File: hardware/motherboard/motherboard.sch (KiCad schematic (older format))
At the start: 21 parts, among them J1 DB37_Female, J10 DB37_Female, J11 DB37_Female, J12 Barrel_Jack, J13 TSR 1-2433, J2 DB37_Female, J3 DB37_Female, J4 DB37_Female, J5 DB37_Female, J6 DB25_Female, J7 DB37_Female, J8 DB25_Female, J9 DB9_Female, SW1 SW_SPST

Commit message: All boards as fabbed at v1.0
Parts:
- added D1, D10, D11, D12, D13, D14, D15, D16, D17, D2, D3, D4, D5, D6, D7, D8, D9: LED, LED_SMD:LED_1206_3216Metric, symbol Device:LED
- added R10, R11, R12, R13, R14, R15, R16, R17, R18, R19, R3, R4, R5, R6, R7, R8, R9: 1K, Resistor_SMD:R_1206_3216Metric, symbol Device:R_US
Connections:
- net GND: now also R10.1, R11.1, R12.1, R13.1, R14.1, R15.1, R16.1, R17.1, R18.1, R19.1, R3.1, R4.1, R5.1, R6.1, R7.1, R8.1, R9.1
- net inst_0: now also D1.2 (A)
- net inst_1: now also D2.2 (A)
- net inst_10: now also D11.2 (A)
- net inst_11: now also D12.2 (A)
- net inst_12: now also D13.2 (A)
- net inst_13: now also D14.2 (A)
- net inst_14: now also D15.2 (A)
- net inst_15: now also D16.2 (A)
- net inst_2: now also D3.2 (A)
- net inst_3: now also D4.2 (A)
- net inst_4: now also D5.2 (A)
- net inst_5: now also D6.2 (A)
- net inst_6: now also D7.2 (A)
- net inst_7: now also D8.2 (A)
- net inst_8: now also D9.2 (A)
- net inst_9: now also D10.2 (A)
- new net: D1.1 (K), R3.2
- new net: D2.1 (K), R4.2
- new net: D3.1 (K), R5.2
- new net: D4.1 (K), R6.2
- new net: D5.1 (K), R7.2
- new net: D6.1 (K), R8.2
- new net: D7.1 (K), R9.2
- new net: D8.1 (K), R10.2
- new net: D9.1 (K), R11.2
- new net: D10.1 (K), R12.2
- new net: D11.1 (K), R13.2
- new net: D12.1 (K), R14.2
- new net: D13.1 (K), R15.2
- new net: D14.1 (K), R16.2
- new net: D15.1 (K), R17.2
- new net: D16.1 (K), R18.2
- new net: D17.1 (K), R19.2
- new net ~inst_15: D17.2 (A)
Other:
- note added: "Instruction LEDs"

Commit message: Motherboard: Added power switch, moved reset switch, modified silkscreens for readability, fixed A-register connector pinout, grounded NC input pins, changed paste layer clearance to -0.05mm
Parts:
- added SW2: SW_SPST, nandirl logo:SPST Toggle Switch, symbol Switch:SW_SPST
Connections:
- net Vin: now also SW2.2 (B); no longer C1.1, J12.1
- net areg_in0: now also J1.18; no longer J1.27
- net areg_in1: now also J1.36; no longer J1.8
- net areg_in10: now also J1.13; no longer J1.22
- net areg_in11: now also J1.31; no longer J1.3
- net areg_in12: now also J1.12; no longer J1.21
- net areg_in13: now also J1.30; no longer J1.2
- net areg_in14: now also J1.11; no longer J1.20
- net areg_in15: now also J1.29; no longer J1.1
- net areg_in2: now also J1.17; no longer J1.26
- net areg_in3: now also J1.35; no longer J1.7
- net areg_in4: now also J1.16; no longer J1.25
- net areg_in5: now also J1.34; no longer J1.6
- net areg_in6: now also J1.15; no longer J1.24
- net areg_in7: now also J1.33; no longer J1.5
- net areg_in8: now also J1.14; no longer J1.23
- net areg_in9: now also J1.32; no longer J1.4
- net areg_out0: now also J1.1; no longer J1.29
- net areg_out1: now also J1.20; no longer J1.11
- net areg_out10: now also J1.6; no longer J1.34
- net areg_out11: now also J1.25; no longer J1.16
- net areg_out12: now also J1.7; no longer J1.35
- net areg_out13: now also J1.26; no longer J1.17
- net areg_out14: now also J1.8; no longer J1.36
- net areg_out15: now also J1.27; no longer J1.18
- net areg_out2: now also J1.2; no longer J1.30
- net areg_out3: now also J1.21; no longer J1.12
- net areg_out4: now also J1.3; no longer J1.31
- net areg_out5: now also J1.22; no longer J1.13
- net areg_out6: now also J1.4; no longer J1.32
- net areg_out7: now also J1.23; no longer J1.14
- net areg_out8: now also J1.5; no longer J1.33
- net areg_out9: now also J1.24; no longer J1.15
- new net: C1.1, J12.1, SW2.1 (A)
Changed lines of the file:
@@
 	1    0    0    -1
 $EndComp
-Text GLabel 13650 3000 0    50   Output ~ 0
+Text GLabel 13650 1100 0    50   Output ~ 0
 areg_out0
-Text GLabel 13650 3100 0    50   Output ~ 0
+Text GLabel 13650 1200 0    50   Output ~ 0
 areg_out1
-Text GLabel 13650 3200 0    50   Output ~ 0
+Text GLabel 13650 1300 0    50   Output ~ 0
 areg_out2
-Text GLabel 13650 3300 0    50   Output ~ 0
+Text GLabel 13650 1400 0    50   Output ~ 0
 areg_out3
-Text GLabel 13650 3400 0    50   Output ~ 0
+Text GLabel 13650 1500 0    50   Output ~ 0
 areg_out4
-Text GLabel 13650 3500 0    50   Output ~ 0
+Text GLabel 13650 1600 0    50   Output ~ 0
 areg_out5
-Text GLabel 13650 3600 0    50   Output ~ 0
+Text GLabel 13650 1700 0    50   Output ~ 0
 areg_out6
-Text GLabel 13650 3700 0    50   Output ~ 0
+Text GLabel 13650 1800 0    50   Output ~ 0
 areg_out7
-Text GLabel 13650 3800 0    50   Output ~ 0
+Text GLabel 13650 1900 0    50   Output ~ 0
 areg_out8
-Text GLabel 13650 3900 0    50   Output ~ 0
+Text GLabel 13650 2000 0    50   Output ~ 0
 areg_out9
-Text GLabel 13650 4000 0    50   Output ~ 0
+Text GLabel 13650 2100 0    50   Output ~ 0
 areg_out10
-Text GLabel 13650 4100 0    50   Output ~ 0
+Text GLabel 13650 2200 0    50   Output ~ 0
 areg_out11
-Text GLabel 13650 4200 0    50   Output ~ 0
+Text GLabel 13650 2300 0    50   Output ~ 0
 areg_out12
-Text GLabel 13650 4300 0    50   Output ~ 0
+Text GLabel 13650 2400 0    50   Output ~ 0
 areg_out13
-Text GLabel 13650 4400 0    50   Output ~ 0
+Text GLabel 13650 2500 0    50   Output ~ 0
 areg_out14
-Text GLabel 13650 4500 0    50   Output ~ 0
+Text GLabel 13650 2600 0    50   Output ~ 0
 areg_out15
-Text GLabel 13650 4500 0    50   Output ~ 0
+Text GLabel 13650 2600 0    50   Output ~ 0
 areg_out15
 $Comp
@@
 	13650 2800 13650 2700
 Connection ~ 13650 2700
-Text GLabel 13650 2600 0    50   Input ~ 0
+Text GLabel 13650 4500 0    50   Input ~ 0
 areg_in0
-Text GLabel 13650 2500 0    50   Input ~ 0
+Text GLabel 13650 4400 0    50   Input ~ 0
 areg_in1
-Text GLabel 13650 2400 0    50   Input ~ 0
+Text GLabel 13650 4300 0    50   Input ~ 0
 areg_in2
-Text GLabel 13650 2300 0    50   Input ~ 0
+Text GLabel 13650 4200 0    50   Input ~ 0
 areg_in3
-Text GLabel 13650 2200 0    50   Input ~ 0
+Text GLabel 13650 4100 0    50   Input ~ 0
 areg_in4
-Text GLabel 13650 2100 0    50   Input ~ 0
+Text GLabel 13650 4000 0    50   Input ~ 0
 areg_in5
-Text GLabel 13650 2000 0    50   Input ~ 0
+Text GLabel 13650 3900 0    50   Input ~ 0
 areg_in6
-Text GLabel 13650 1900 0    50   Input ~ 0
+Text GLabel 13650 3800 0    50   Input ~ 0
 areg_in7
-Text GLabel 13650 1800 0    50   Input ~ 0
+Text GLabel 13650 3700 0    50   Input ~ 0
 areg_in8
-Text GLabel 13650 1700 0    50   Input ~ 0
+Text GLabel 13650 3600 0    50   Input ~ 0
 areg_in9
-Text GLabel 13650 1600 0    50   Input ~ 0
+Text GLabel 13650 3500 0    50   Input ~ 0
 areg_in10
-Text GLabel 13650 1500 0    50   Input ~ 0
+Text GLabel 13650 3400 0    50   Input ~ 0
 areg_in11
-Text GLabel 13650 1400 0    50   Input ~ 0
+Text GLabel 13650 3300 0    50   Input ~ 0
 areg_in12
-Text GLabel 13650 1300 0    50   Input ~ 0
+Text GLabel 13650 3200 0    50   Input ~ 0
 areg_in13
-Text GLabel 13650 1200 0    50   Input ~ 0
+Text GLabel 13650 3100 0    50   Input ~ 0
 areg_in14
-Text GLabel 13650 1100 0    50   Input ~ 0
+Text GLabel 13650 3000 0    50   Input ~ 0
 areg_in15
 Text GLabel 13650 4600 0    50   Input ~ 0
@@
 	1    0    0    -1
 $EndComp
-Text GLabel 9350 9550 2    50   Output ~ 0
+Text GLabel 9900 9550 2    50   Output ~ 0
 Vin
 Wire Wire Line
@@
 Text Notes 9650 5650 2    50   ~ 0
 Instruction LEDs
+$Comp
+L Switch:SW_SPST SW2
+U 1 1 5EDCC3F6
+P 9550 9550
+F 0 "SW2" H 9550 9785 50  0000 C CNN
+F 1 "SW_SPST" H 9550 9694 50  0000 C CNN
+F 2 "nandirl logo:SPST Toggle Switch" H 9550 9550 50  0001 C CNN
+F 3 "~" H 9550 9550 50  0001 C CNN
+F 4 "EG4914-ND" H 9550 9550 50  0001 C CNN "Digikey PN"
+	1    9550 9550
+	1    0    0    -1
+$EndComp
+Wire Wire Line
+	9750 9550 9900 9550
 $EndSCHEMATC

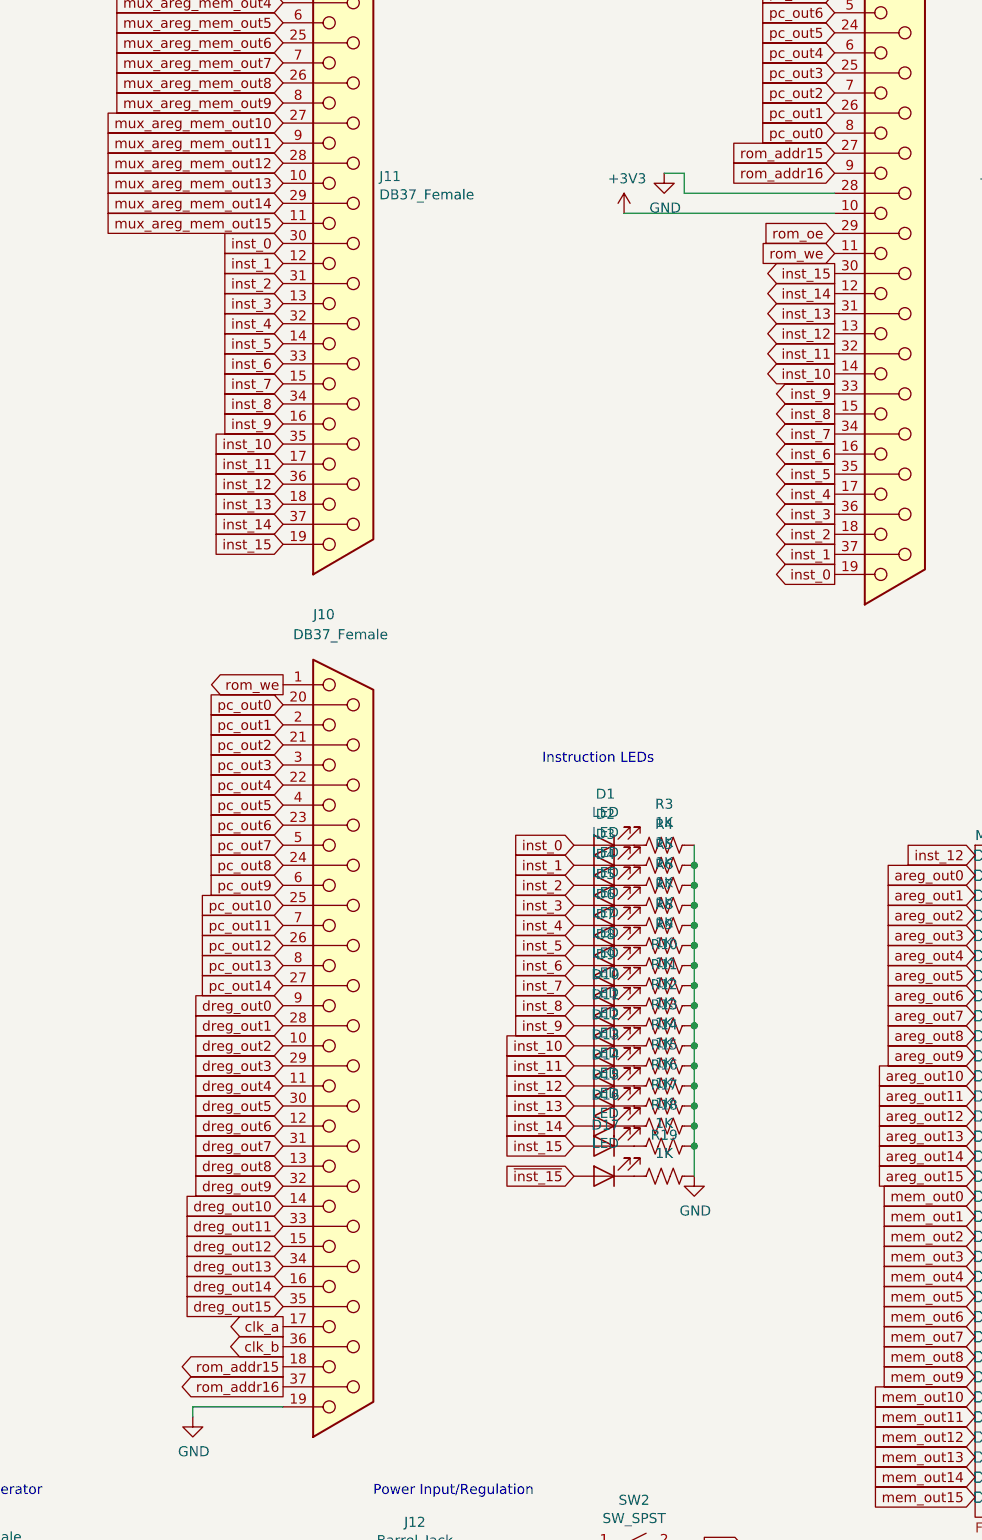
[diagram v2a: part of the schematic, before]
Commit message: Debugger updated to Teensy 4.1 with magjack for ethernet. Updated motherboard<>debugger pinout to include 3.3v source
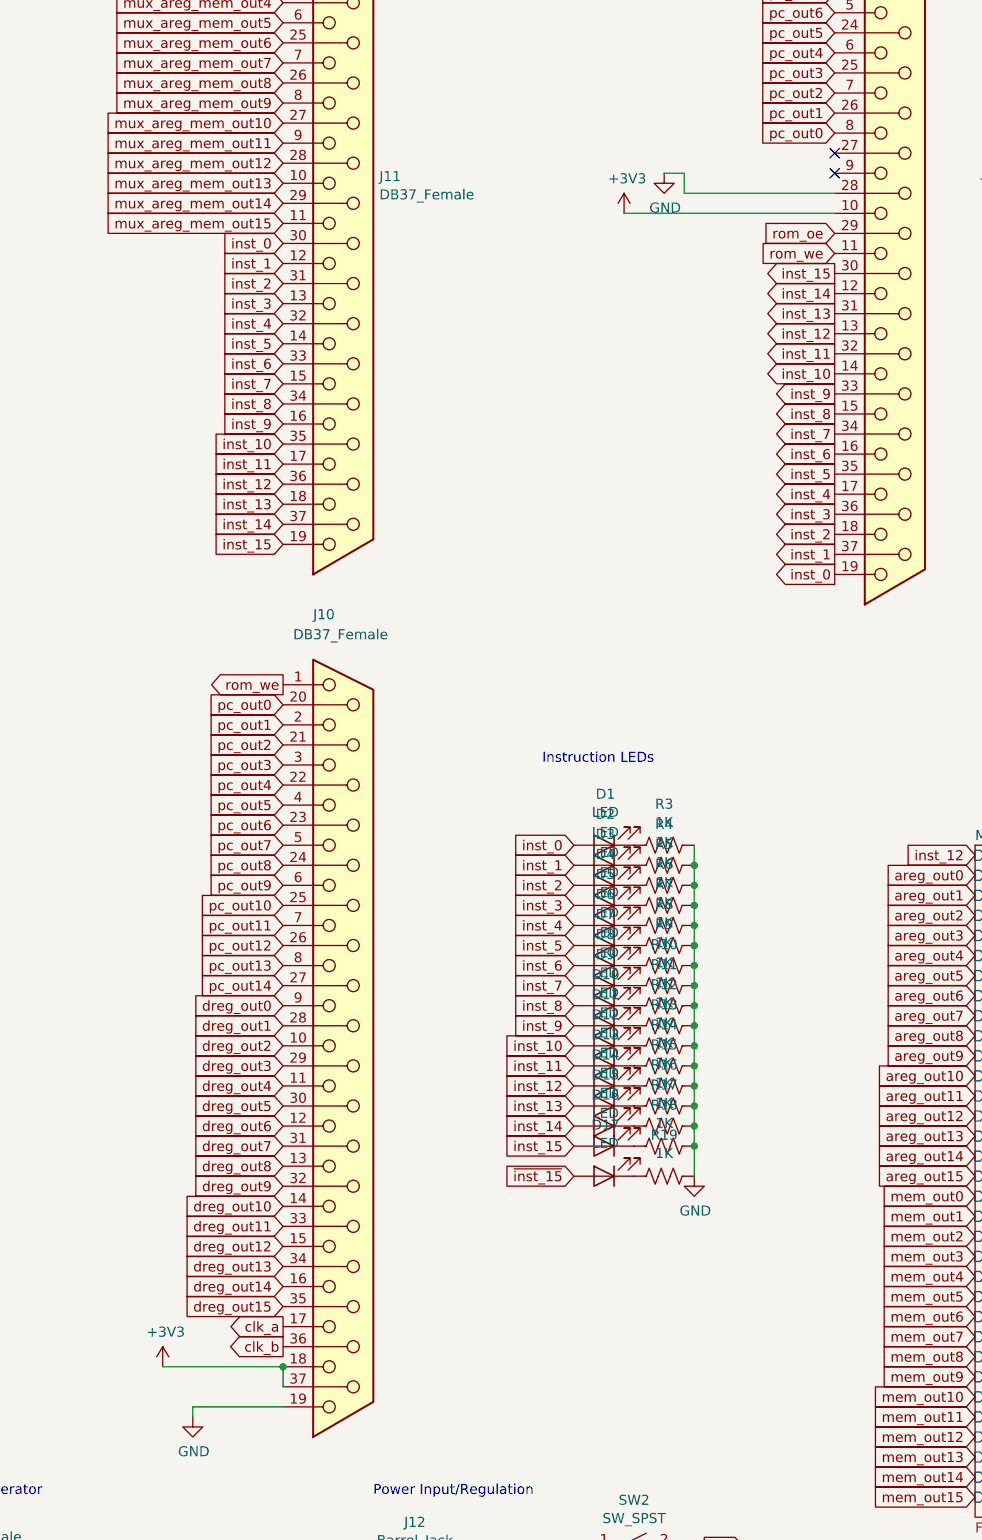
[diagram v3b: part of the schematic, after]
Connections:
- net +3V3: now also J10.18, J10.37
- net rom_addr15: no longer names the net of J4.27
- net rom_addr15: no longer J10.18
- net rom_addr16: no longer names the net of J4.9
- net rom_addr16: no longer J10.37
- no-connect marks 6 -> 8
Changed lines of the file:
@@
 Wire Wire Line
 	4000 9800 4000 9900
-Text GLabel 10550 2600 0    50   Input ~ 0
-rom_addr15
 Wire Wire Line
 	9800 2800 9800 2700
@@
 Wire Wire Line
 	9500 2900 10550 2900
-Text GLabel 10550 2700 0    50   Input ~ 0
-rom_addr16
 Text GLabel 10550 3000 0    50   Input ~ 0
 rom_oe
@@
 Text GLabel 7800 5250 0    50   Output ~ 0
 rom_we
-Text GLabel 7800 8650 0    50   Output ~ 0
-rom_addr15
-Text GLabel 7800 8750 0    50   Output ~ 0
-rom_addr16
 Wire Wire Line
 	7800 8850 7350 8850
@@
 Wire Wire Line
 	9750 9550 9900 9550
+Wire Wire Line
+	7800 8750 7800 8650
+Wire Wire Line
+	7800 8650 7200 8650
+Connection ~ 7800 8650
+$Comp
+L power:+3V3 #PWR0129
+U 1 1 5F572908
+P 7200 8650
+F 0 "#PWR0129" H 7200 8500 50  0001 C CNN
+F 1 "+3V3" H 7215 8823 50  0000 C CNN
+F 2 "" H 7200 8650 50  0001 C CNN
+F 3 "" H 7200 8650 50  0001 C CNN
+	1    7200 8650
+	1    0    0    -1
+$EndComp
+NoConn ~ 10550 2600
+NoConn ~ 10550 2700
 $EndSCHEMATC
